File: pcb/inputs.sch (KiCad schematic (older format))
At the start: 83 parts, among them U11 MPXA6115AC6U, U4 MAX9926UAEE+, U6 MPXA4250AC6U

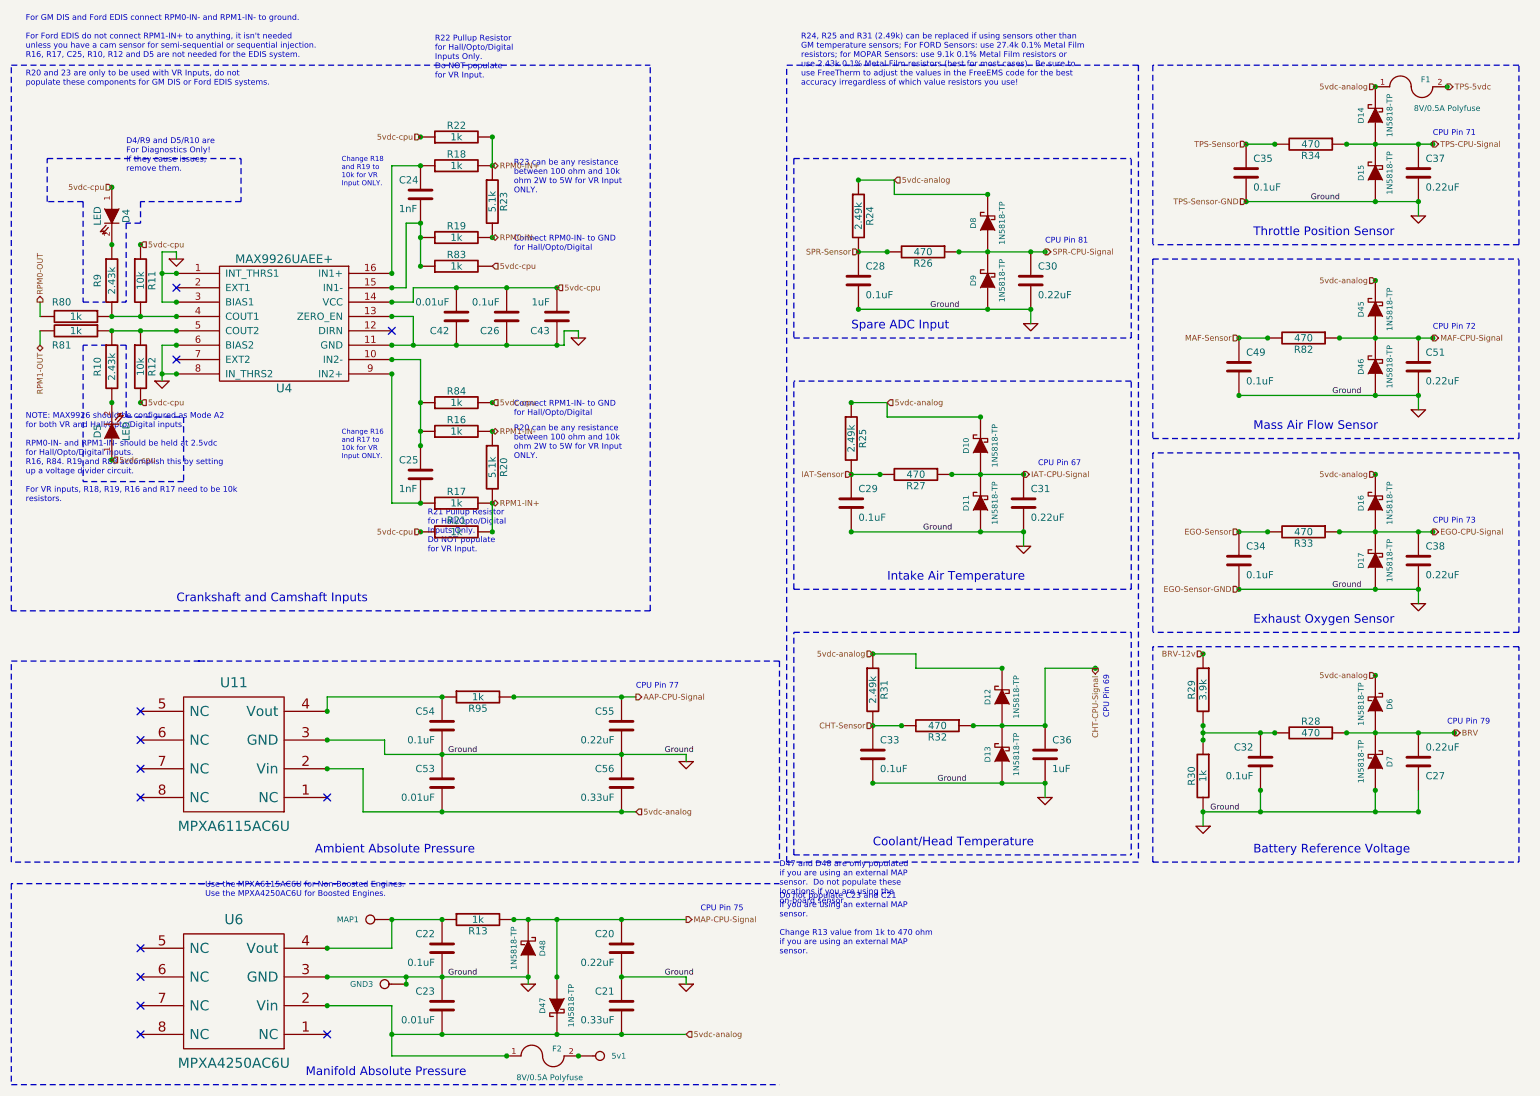
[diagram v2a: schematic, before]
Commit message: Renamed F1 and F2 from Polyfuse to 8v/0.50A PTC Resettable Fuse on the schematics to match the Bill-of-Materials (BOM).
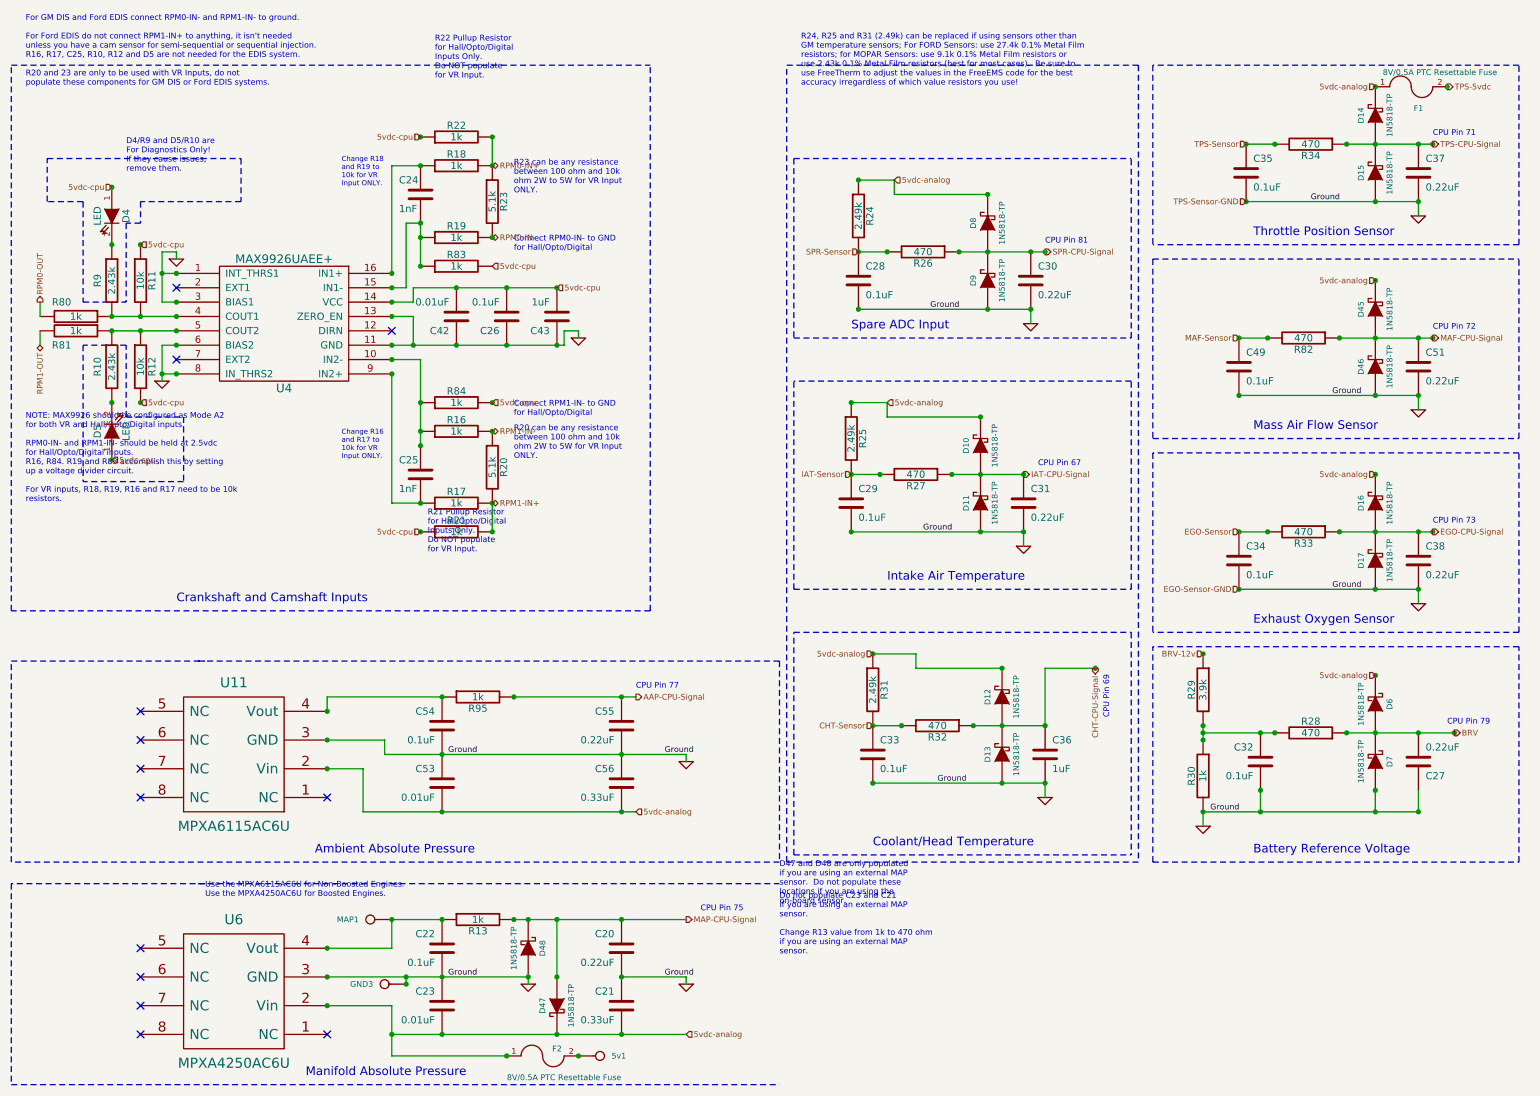
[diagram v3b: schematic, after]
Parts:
- F1, F2: value 8V/0.5A Polyfuse -> 8V/0.5A PTC Resettable Fuse
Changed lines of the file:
@@
 Sheet 4 7
 Title "Jaguar PCB for FreeEMS"
-Date "4 aug 2014"
+Date "6 aug 2014"
 Rev "0.7-alpha"
 Comp "Git: f0f0026dbb"
@@
 U 1 1 51A67DEA
 P 10300 750
-F 0 "F1" H 10400 800 40  0000 C CNN
-F 1 "8V/0.5A Polyfuse" H 10550 600 40  0000 C CNN
+F 0 "F1" H 10350 600 40  0000 C CNN
+F 1 "8V/0.5A PTC Resettable Fuse" H 10500 850 40  0000 C CNN
 F 2 "" H 10300 750 60  0001 C CNN
 F 3 "" H 10300 750 60  0001 C CNN
@@
 P 4250 7500
 F 0 "F2" H 4350 7550 40  0000 C CNN
-F 1 "8V/0.5A Polyfuse" H 4300 7350 40  0000 C CNN
+F 1 "8V/0.5A PTC Resettable Fuse" H 4400 7350 40  0000 C CNN
 F 2 "" H 4250 7500 60  0001 C CNN
 F 3 "" H 4250 7500 60  0001 C CNN

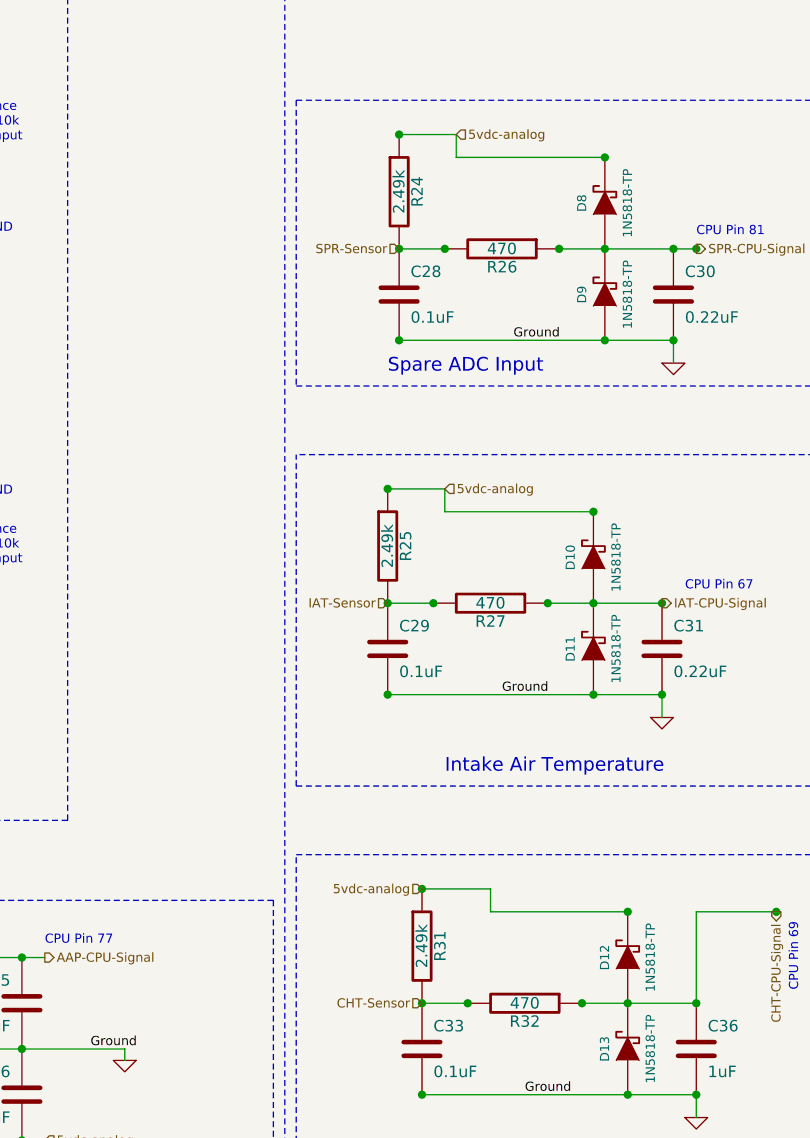
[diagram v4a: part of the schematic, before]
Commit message: Changed R24, R25 and R31 from 2.49k 0.1% resistors to 2.7k 0.1% resistors as this is a good compromise for Denso/GM thermistors.
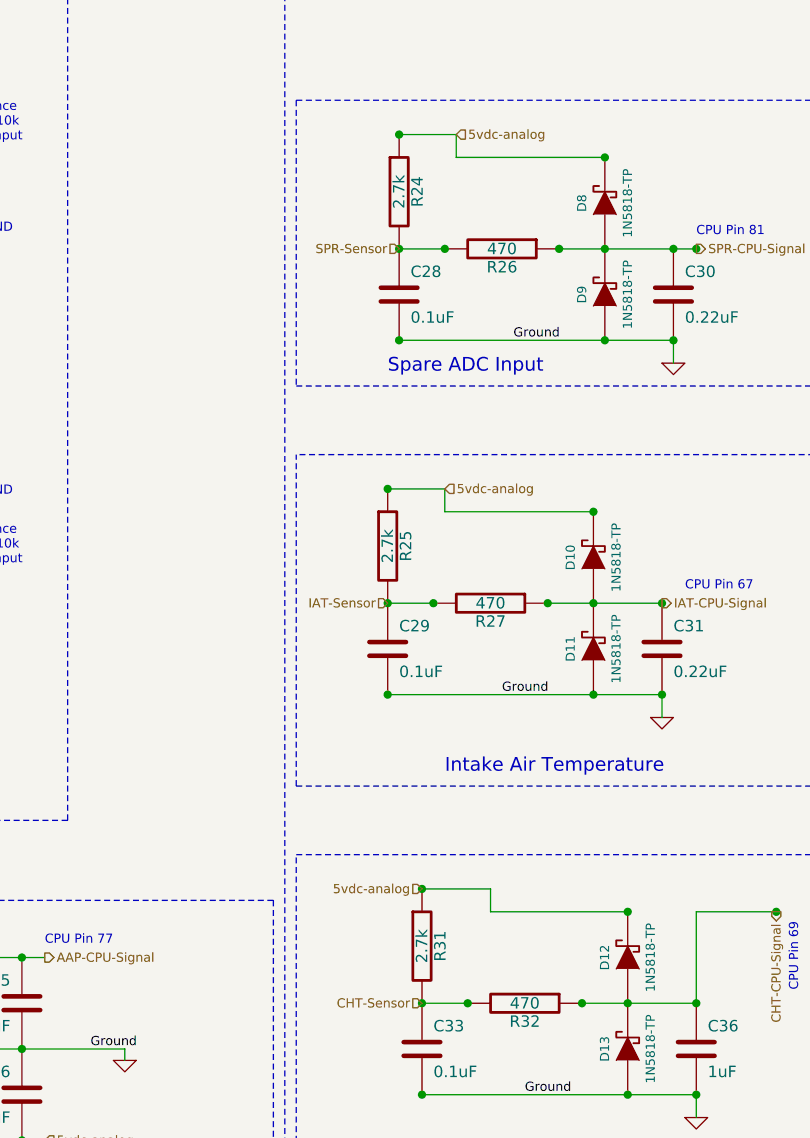
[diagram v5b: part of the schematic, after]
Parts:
- R24, R25, R31: value 2.49k -> 2.7k
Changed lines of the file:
@@
 Sheet 4 7
 Title "Jaguar PCB for FreeEMS"
-Date "23 oct 2014"
+Date "14 apr 2015"
 Rev "0.7-alpha"
 Comp "Git: f0f0026dbb"
@@
 P 6550 4950
 F 0 "R31" V 6630 4950 50  0000 C CNN
-F 1 "2.49k" V 6550 4950 50  0000 C CNN
+F 1 "2.7k" V 6550 4950 50  0000 C CNN
 F 2 "" H 6550 4950 60  0001 C CNN
 F 3 "" H 6550 4950 60  0001 C CNN
@@
 P 6400 3200
 F 0 "R25" V 6480 3200 50  0000 C CNN
-F 1 "2.49k" V 6400 3200 50  0000 C CNN
+F 1 "2.7k" V 6400 3200 50  0000 C CNN
 F 2 "" H 6400 3200 60  0001 C CNN
 F 3 "" H 6400 3200 60  0001 C CNN
@@
 P 6450 1650
 F 0 "R24" V 6530 1650 50  0000 C CNN
-F 1 "2.49k" V 6450 1650 50  0000 C CNN
+F 1 "2.7k" V 6450 1650 50  0000 C CNN
 F 2 "" H 6450 1650 60  0001 C CNN
 F 3 "" H 6450 1650 60  0001 C CNN

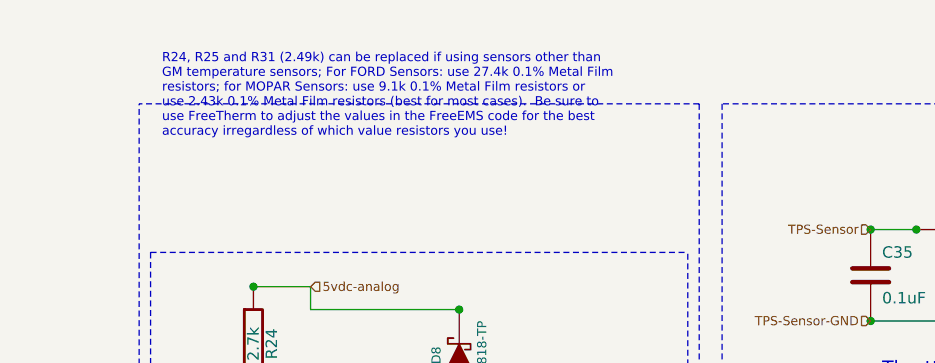
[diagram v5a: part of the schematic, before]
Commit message: Moved D5 and D34 from the green LED part number to the red LED part number in the BOM, changed D30 and D41 from the red LED part number to the green LED part number in the BOM.  Changed wording for the thermistor bias resistors to show 2.7k resistors for most sensors including Denso/GM sensors.
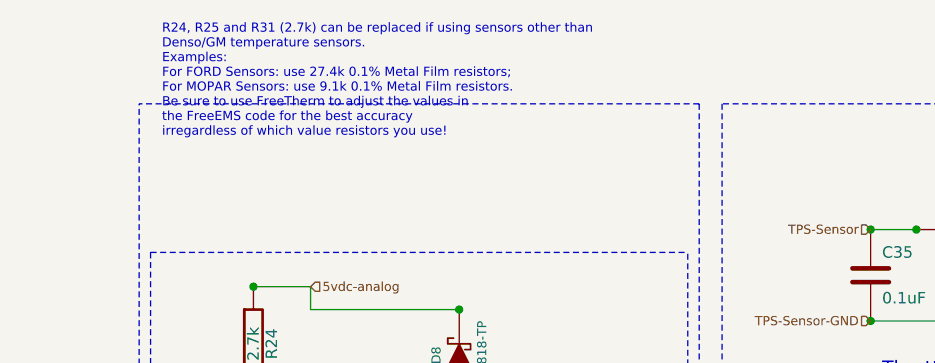
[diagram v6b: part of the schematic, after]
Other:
- note added: "R24, R25 and R31 (2.7k) can be replaced if using sensors other than\nDenso/GM temperature sensors.\nExamples:\nFor FORD Sensors: use 27.4k 0.1% Metal Film resistors; \nFor MOPAR Sensors: use 9.1k 0.1% Metal Film resistors.\nBe sure to use FreeTherm to adjust the values in\nthe FreeEMS code for the best accuracy \nirregardless of which value resistors you use!"
- note removed: "R24, R25 and R31 (2.49k) can be replaced if using sensors other than\nGM temperature sensors; For FORD Sensors: use 27.4k 0.1% Metal Film\nresistors; for MOPAR Sensors: use 9.1k 0.1% Metal Film resistors or \nuse 2.43k 0.1% Metal Film resistors (best for most cases). Be sure to\nuse FreeTherm to adjust the values in the FreeEMS code for the best\naccuracy irregardless of which value resistors you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"
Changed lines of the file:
@@
 Use the MPXA6115AC6U for Non-Boosted Engines.\nUse the MPXA4250AC6U for Boosted Engines.
 Text Notes 6050 750  0    40   ~ 0
-R24, R25 and R31 (2.49k) can be replaced if using sensors other than\nGM temperature sensors; For FORD Sensors: use 27.4k 0.1% Metal Film\nresistors; for MOPAR Sensors: use 9.1k 0.1% Metal Film resistors or \nuse 2.43k 0.1% Metal Film resistors (best for most cases).  Be sure to\nuse FreeTherm to adjust the values in the FreeEMS code for the best\naccuracy irregardless of which value resistors you use!
+R24, R25 and R31 (2.7k) can be replaced if using sensors other than\nDenso/GM temperature sensors.\nExamples:\nFor FORD Sensors: use 27.4k 0.1% Metal Film resistors; \nFor MOPAR Sensors: use 9.1k 0.1% Metal Film resistors.\nBe sure to use FreeTherm to adjust the values in\nthe FreeEMS code for the best accuracy \nirregardless of which value resistors you use!
 Text Notes 650  750  0    40   ~ 0
 For GM DIS and Ford EDIS connect RPM0-IN- and RPM1-IN- to ground.\n\nFor Ford EDIS do not connect RPM1-IN+ to anything, it isn't needed\nunless you have a cam sensor for semi-sequential or sequential injection. \nR16, R17, C25, R10, R12 and D5 are not needed for the EDIS system.\n\nR20 and 23 are only to be used with VR Inputs, do not\npopulate these components for GM DIS or Ford EDIS systems.

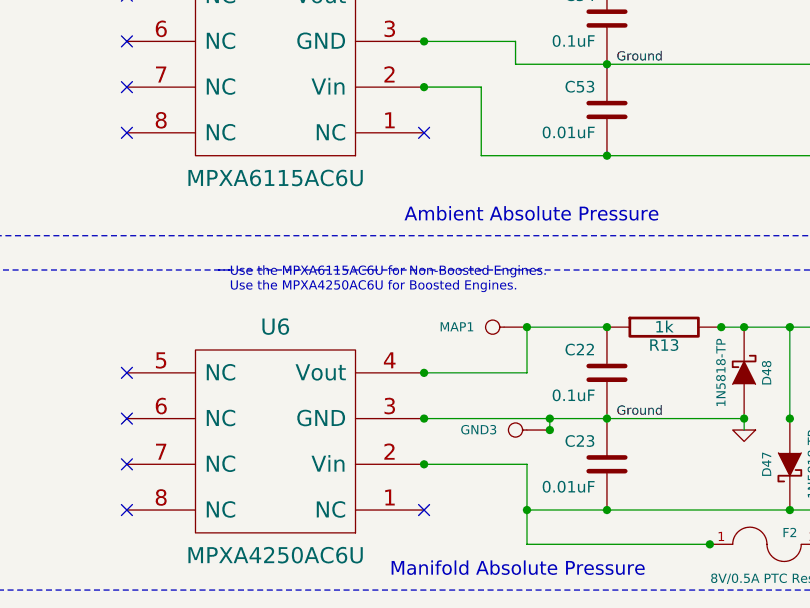
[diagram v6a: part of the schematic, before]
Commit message: Changed AAP and MAP sensors from SOP-8 to SSOP-8 package.
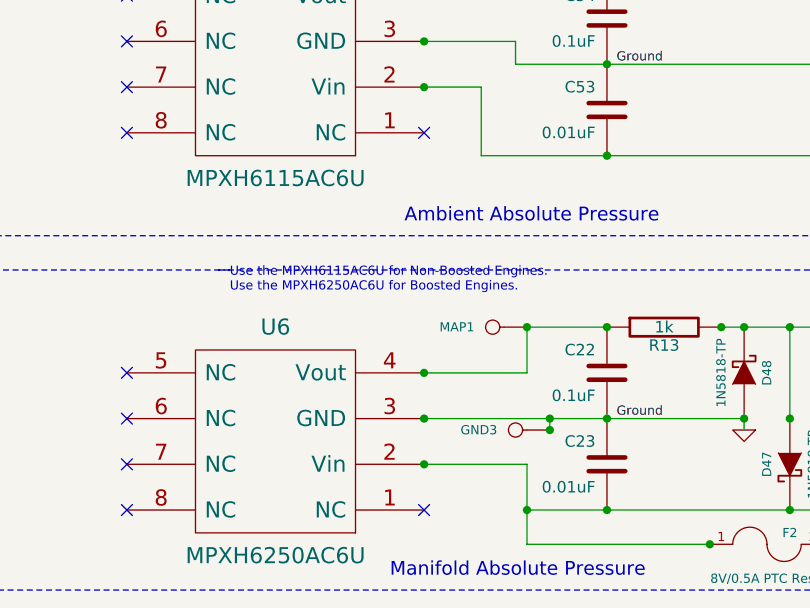
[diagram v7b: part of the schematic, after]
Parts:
- U11: value MPXA6115AC6U -> MPXH6115AC6U
- U6: value MPXA4250AC6U -> MPXH6250AC6U
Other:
- note added: "Use the MPXH6115AC6U for Non-Boosted Engines.\nUse the MPXH6250AC6U for Boosted Engines."
- note removed: "Use the MPXA6115AC6U for Non-Boosted Engines.\nUse the MPXA4250AC6U for Boosted Engines."
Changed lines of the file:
@@
 Sheet 4 7
 Title "Jaguar PCB for FreeEMS"
-Date "14 apr 2015"
+Date "13 may 2015"
 Rev "0.7-alpha"
 Comp "Git: f0f0026dbb"
@@
 P 2100 7050
 F 0 "U6" H 2100 7550 70  0000 C CNN
-F 1 "MPXA4250AC6U" H 2100 6550 70  0000 C CNN
+F 1 "MPXH6250AC6U" H 2100 6550 70  0000 C CNN
 F 2 "" H 2100 7050 60  0001 C CNN
 F 3 "" H 2100 7050 60  0001 C CNN
@@
 P 2100 5400
 F 0 "U11" H 2100 5900 70  0000 C CNN
-F 1 "MPXA6115AC6U" H 2100 4900 70  0000 C CNN
+F 1 "MPXH6115AC6U" H 2100 4900 70  0000 C CNN
 F 2 "" H 2100 5400 60  0001 C CNN
 F 3 "" H 2100 5400 60  0001 C CNN
@@
 5vdc-analog
 Text Notes 1900 6400 0    40   ~ 0
-Use the MPXA6115AC6U for Non-Boosted Engines.\nUse the MPXA4250AC6U for Boosted Engines.
+Use the MPXH6115AC6U for Non-Boosted Engines.\nUse the MPXH6250AC6U for Boosted Engines.
 Text Notes 6050 750  0    40   ~ 0
 R24, R25 and R31 (2.7k) can be replaced if using sensors other than\nDenso/GM temperature sensors.\nExamples:\nFor FORD Sensors: use 27.4k 0.1% Metal Film resistors; \nFor MOPAR Sensors: use 9.1k 0.1% Metal Film resistors.\nBe sure to use FreeTherm to adjust the values in\nthe FreeEMS code for the best accuracy \nirregardless of which value resistors you use!
